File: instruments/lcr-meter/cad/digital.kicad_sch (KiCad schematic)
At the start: 39 parts, among them J1 USB-C, J4 SWD CLK / DATA, J5 SWD GND / VTREF, J6 UART TX / RX, SW1 BOOTSEL, SW2 RESET, U1 RP2040, U2 W25Q16JVSSIQ, Y1 12MHz CL10pF

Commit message: lcr-meter Rev D: +12 V / -12 V rail monitors on RP2040 ADC0/ADC1
- MON12 (GPIO26, U1.38): R97 100k from 12V (tapped by a via on the In2 12V
  trunk at 109.01,112.6) to R98 10k + C110 100nF to GND at U1: ~1.09 V at
  12 V.
- MON_N12 (GPIO27, U1.39): R100 150k from -12V (T onto the F.Cu -12V trunk
  at x 124.95) to R99 10k to 3V3 + C111 100nF at U1: ~2.3 V at -12 V,
  3.1 V if the rail is absent, never negative while 3V3 is up.
- Divider top resistors sit at the rail ends, so the long B.Cu runs carry
  only a 100k/150k-limited node; filter caps sit at the ADC pins. MON12
  passes west of the 3V3 via; MON_N12 hops the B.Cu 3V3 trunk on In2.
  Reuses existing BOM lines only (C25803, C25804, C22807, C14663).

rebuild.sh: ERC 0, DRC 0, 0 unconnected, parity 0.

Co-Authored-By: Claude Opus 5.5 <noreply@anthropic.com>
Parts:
- added C110, C111: 100nF 50V, LCR:C_0603_1608Metric, symbol LCR:C
- added R98, R99: 10k, LCR:R_0603_1608Metric, symbol LCR:R
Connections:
- net 3V3: now also R99.1
- net GND: now also C110.1, C111.1, R98.1
- net MON12: now reaches U1.38 (GPIO26)
- net MON12: now also C110.2, R98.2
- net MON_N12: now reaches U1.39 (GPIO27)
- net MON_N12: now also C111.2, R99.2
- no-connect marks 16 -> 14

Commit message: lcr-meter Rev D: apply Tier 1 audit fixes
Hand-routed layout edits (cad/tools/edit_lib.py, no autorouter):
- Vias in every exposed pad: U1 8, U8/U9/U10 5, U11/U12 6 (were 0), U13 9.
- ADS9224R: 10 uF X7R 0805 reference caps at 1.56 mm, REFM joined to the
  cap before its via; 1 uF AVDD caps at 1.67/2.46 mm from pins 12/29.
- TPS7A4901/TPS7A3001: support parts packed per TI layout; FB nodes
  13.2/12.0 -> 5.2/5.3 mm, NR 2.1 mm. LDOIN_N In2 run moved off the pads.
- TPS65131 dividers compacted: CONV_FBP 13.1 -> 9.1 mm, CONV_FBN 16.8 -> 12.3 mm.
- RP2040: 1 uF at VREG_VIN (C5).

Parts: red status LED, basic ferrites, W25Q128JV flash (stock), C84,
CL32B106KBJNNNE on the 14 V and converter-input caps, C18/C103 basic,
C36 1 uF -> 100 nF. Extended lines 34 -> 30.

Firmware: settle max(150 ms, 20 cycles); BOOT -> reset_usb_boot().
Host 0.7.0: `temper-lcr boot PORT`.

Withdrawn after checking: converter dividers to TI example values (VPOS
15.105 V at the tolerance stack), 1 % LDO dividers (U12 headroom 0.74 V),
SRV05-4 (pinout unverifiable). regulator_check.py now reads design.json
instead of stale Rev C values.

DRC 0, unconnected 0, parity 0, ERC 0; independent check 576 pins, 0
findings; host 29 tests pass.

Co-Authored-By: Claude Opus 5.5 <noreply@anthropic.com>
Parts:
- C5: value 100nF 50V -> 1uF 50V X5R; LCSC C14663 -> C15849; MPN CC0603KRX7R9BB104 -> CL10A105KB8NNNC; Manufacturer YAGEO -> Samsung Electro-Mechanics; Unit_USD 0.0084 -> 0.0153
- D4: value GREEN -> RED; LCSC C22371297 -> C2286; MPN PSC-1608U52GC-G4 -> KT-0603R; Manufacturer HONGLITRONIC(Hongli Zhihui (HONGLITRONIC)) -> Hubei KENTO Elec; Unit_USD 0.0147 -> 0.0073
- U2: value W25Q16JVSSIQ -> W25Q128JVSIQ; LCSC C131025 -> C97521; MPN W25Q16JVSSIQ -> W25Q128JVSIQ; Unit_USD 1.42 -> 2.4501

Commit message: feat(lcr): Rev E board with TAC5112 codec front end and relay ranges
Hand-routed Rev E on the Rev D outline:
- removes the ADS9224R, AD9833, both THS4551s, FB2 and JP1-JP6;
- adds the TAC5112 with its own AP2112K for 3V3A, three TQ2SA latching
  relays and their AO3400A drivers.

cad/tools/rev_e.py builds design.json and routing.json from the Rev D
package. rev_e_routes.py gives every new segment and via by coordinate.

Details:
- Every via is now a 0.3 mm drill with a pad of 0.45 mm or more.
  The board rules set a 0.30 mm minimum hole and a 0.075 mm minimum
  annular ring.
- Basic-library swaps: D1 is now SRV05-4, and SW1/SW2 are now TS-1088.
- placement_offsets.py adds JLC CPL offsets for the new keyed parts,
  read from the lceda.cn EasyEDA mirror (easyeda.com returns 403). It
  reproduces the audited offsets for U3 (270) and Q1 (180).

Checks:
- rebuild.sh: ERC 0, DRC 0 violations and 0 unconnected, parity 0.
- package_cad and audit_dfm pass: 34 intended via-in-pad, none
  unexpected.
- independent_check.py e: 575 pins, 0 findings.

Co-Authored-By: Claude Opus 5.5 <noreply@anthropic.com>
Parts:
- removed R11: 33R, LCR:R_0603_1608Metric, symbol LCR:R
- D1: value USBLC6-2SC6 -> SRV05-4; LCSC C7519 -> C7420376; MPN USBLC6-2SC6 -> SRV05-4; Manufacturer STMicroelectronics -> hongjiacheng; Unit_USD 0.1776 -> 0.0851
- SW1, SW2: footprint LCR:SW_SPST_B3U-1000P -> LCR:SW_SPST_TS-1088-xR020; LCSC C231329 -> C720477; MPN B3U-1000P -> TS-1088-AR02016; Manufacturer Omron Electronics -> XUNPU; Unit_USD 0.1875 -> 0.0527
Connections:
- net ADC_CONVST renamed RNG_SET_HI
- net ADC_CS renamed I2S_BCLK
- net ADC_READY: no longer names the net of U1.15 (GPIO12)
- net ADC_RESET renamed I2C_SDA
- net ADC_SCLK renamed I2S_FSYNC
- net ADC_SDI renamed RNG_SET_LO
- net ADC_SDO_A renamed I2S_DIN
- net ADC_SDO_B renamed I2S_DOUT
- net DDS_CLK_RAW: no longer names the net of U1.32 (GPIO21)
- net DDS_FSYNC renamed I2C_SCL
- net DDS_SCLK renamed RNG_RESET
- net DDS_SDATA renamed RNG_SET_MED
- no-connect marks 14 -> 16
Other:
- moved on the sheet: C1, C10, C11, C110, C111, C12, C13, C14, C15, C2, C3, C4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

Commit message: Rev E board: four-terminal BNC jacks, K4 reference relay
- J3 header -> four SAMZO BNC-KYWE-295-W4-N (C41416668, hand fit) on the
  top edge at 22 mm pitch: J3 HCUR (DUT_HI), J7 HPOT, J8 LPOT, J9 LCUR
  (DUT_LO). Followers U6.5/U7.5 now sense HPOT/LPOT. R105/R106 1k (basic
  C21190) tie POT to CUR for two-terminal leads. Board 140 x 105 mm.
- K4 TQ2SA: COM2 = HCUR, NO2 -> R107 1k 0.1 % -> LCUR; RESET on the
  shared RLY_RST, SET on Q6/GPIO14 (GPIO12's pad is boxed in by USB_SENSE).
- C78 moves onto the LCUR run. All copper hand-specified in rev_e_routes.py.
- rebuild: ERC 0, DRC 0 / 0 unconnected, parity PASS; independent_check
  620 pins, 0 findings (topology check updated for 4T).
- Five boards $453.46 (+$36.87); 5 PCBs / 2 assembled $309.31.

Co-Authored-By: Claude Opus 5.5 <noreply@anthropic.com>
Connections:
- net RNG_SET_REF: now reaches U1.17 (GPIO14)
- no-connect marks 16 -> 15

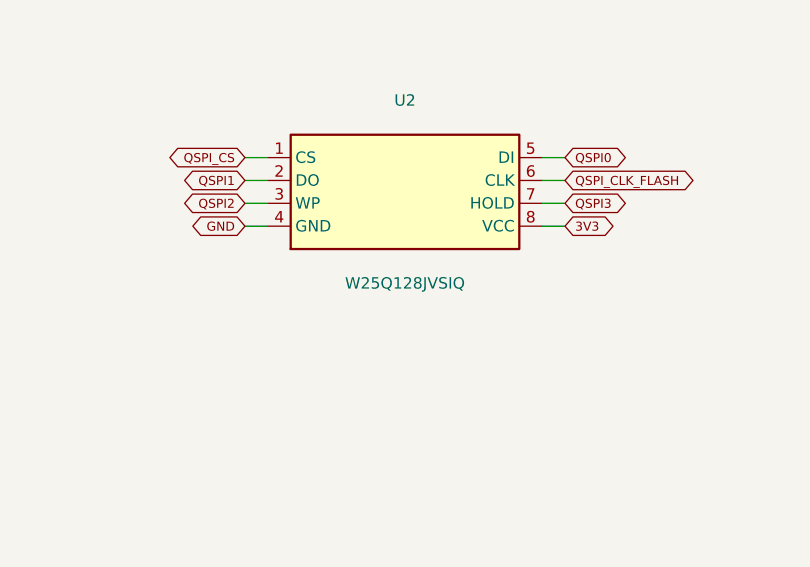
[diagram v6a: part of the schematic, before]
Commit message: lcr-meter: Rev E consolidates four extended lines and moves U2 to a 2 MB flash
LDO dividers: U11 82k/9.1k 1 % basic; U12 100k over 5k+1k+5k from 0.1 % lines
already on the BOM (R112 added). C34/C35 270 pF built as two 560 pF in series
(C114/C115). R83 1.74M built as 240k + 1.5M (R111). U2 W25Q128JVSIQ ->
GD25Q16ESIGR, same SOP-8 208 mil land, CPL offset unchanged.

regulator_check reads divider strings from the netlist and adds a TCR row:
45 of 46 pass; R95/R96 headroom 1.083 V (was the 0.951 V FLAG); the new TCR row
flags 0.970 V (0.838 V on the old dividers). New source_stage.py: U5 margin
59.73 deg (60.13), -0.025 dB at 85 kHz. ERC 0, DRC 0/0/0, independent check
632 pins 0 findings. 23 extended lines; five boards $428.40 -> $408.57.

Co-Authored-By: Claude Opus 5.5 <noreply@anthropic.com>
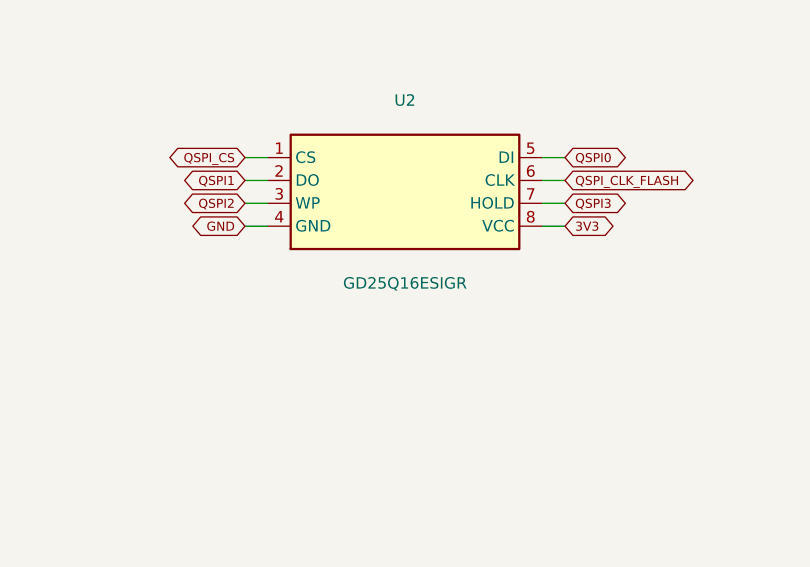
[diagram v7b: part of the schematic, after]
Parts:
- U2: value W25Q128JVSIQ -> GD25Q16ESIGR; LCSC C97521 -> C2922792; MPN W25Q128JVSIQ -> GD25Q16ESIGR; Manufacturer Winbond Elec -> GigaDevice; Unit_USD 2.4501 -> 0.6011

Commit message: lcr-meter: J4-J6 do not fit (USB boot from blank flash); FR4-Standard TG 135-140 instead of TG155
RP2040 datasheet 2.8: a blank flash fails the boot2 CRC and the bootrom drops to
USB mass storage, so the first UF2 loads over USB; the header lands stay. J4-J6
are DNP in the schematic, PCB and BOM, and order_estimate skips DNP parts. TG155
is dropped for JLC's 4-layer default; the 7628 stackup used by the parasitic
extraction is unchanged. ERC 0, DRC 0/0/0, independent check 0 findings.
Five boards $408.57 -> $396.25.

Co-Authored-By: Claude Opus 5.5 <noreply@anthropic.com>
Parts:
- J4, J5, J6: Assembly Hand fit -> DNP; now not fitted
